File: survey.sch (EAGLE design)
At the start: 18 parts

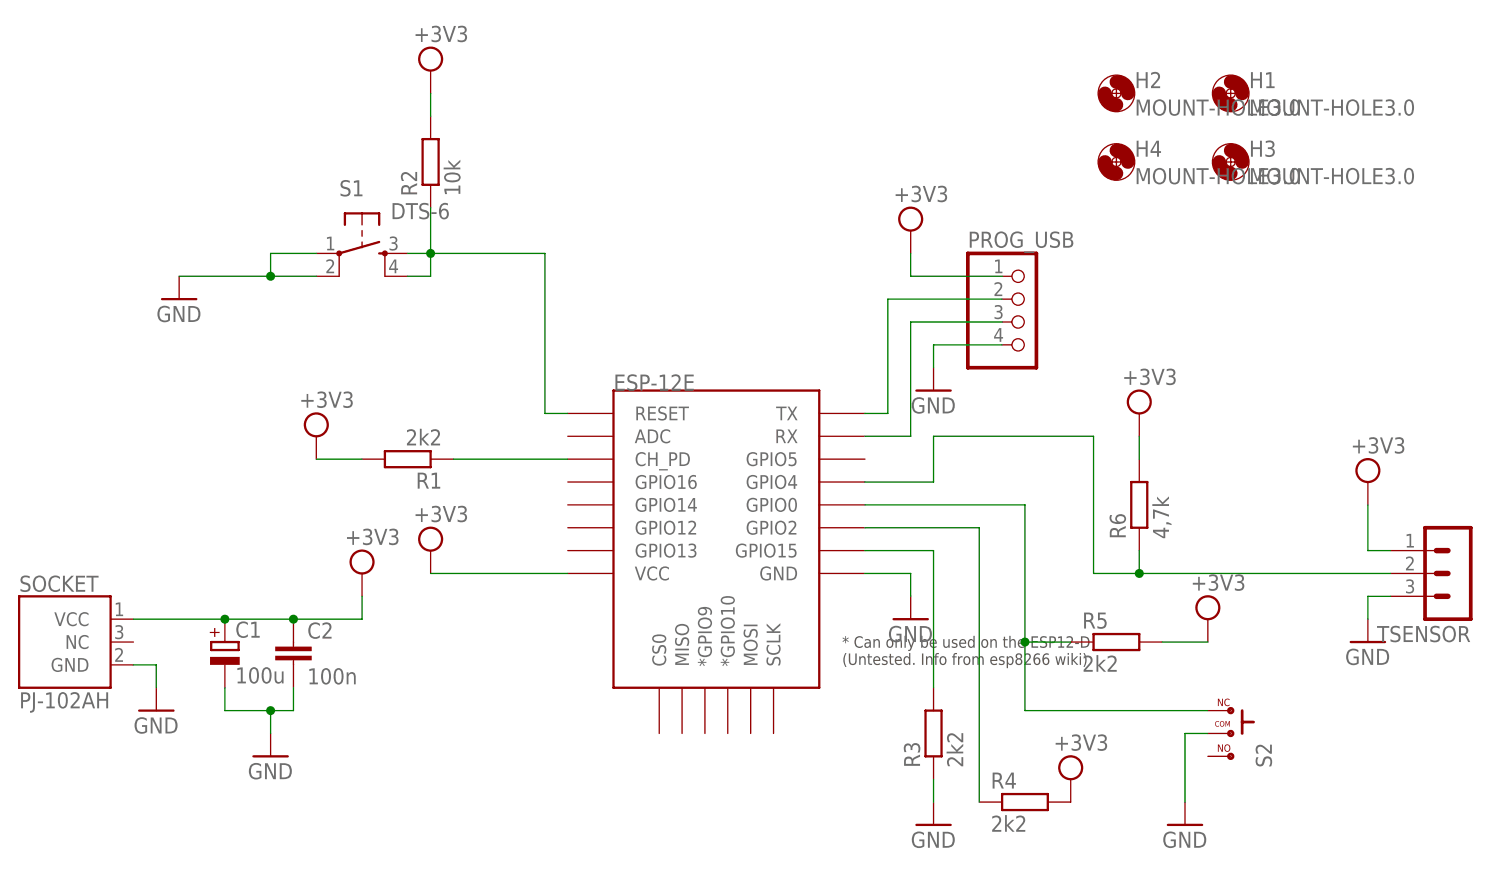
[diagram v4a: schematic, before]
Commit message: Changed some resistors from 10k for 2k2 and added resisors 100 to reset and gpio0 pin.
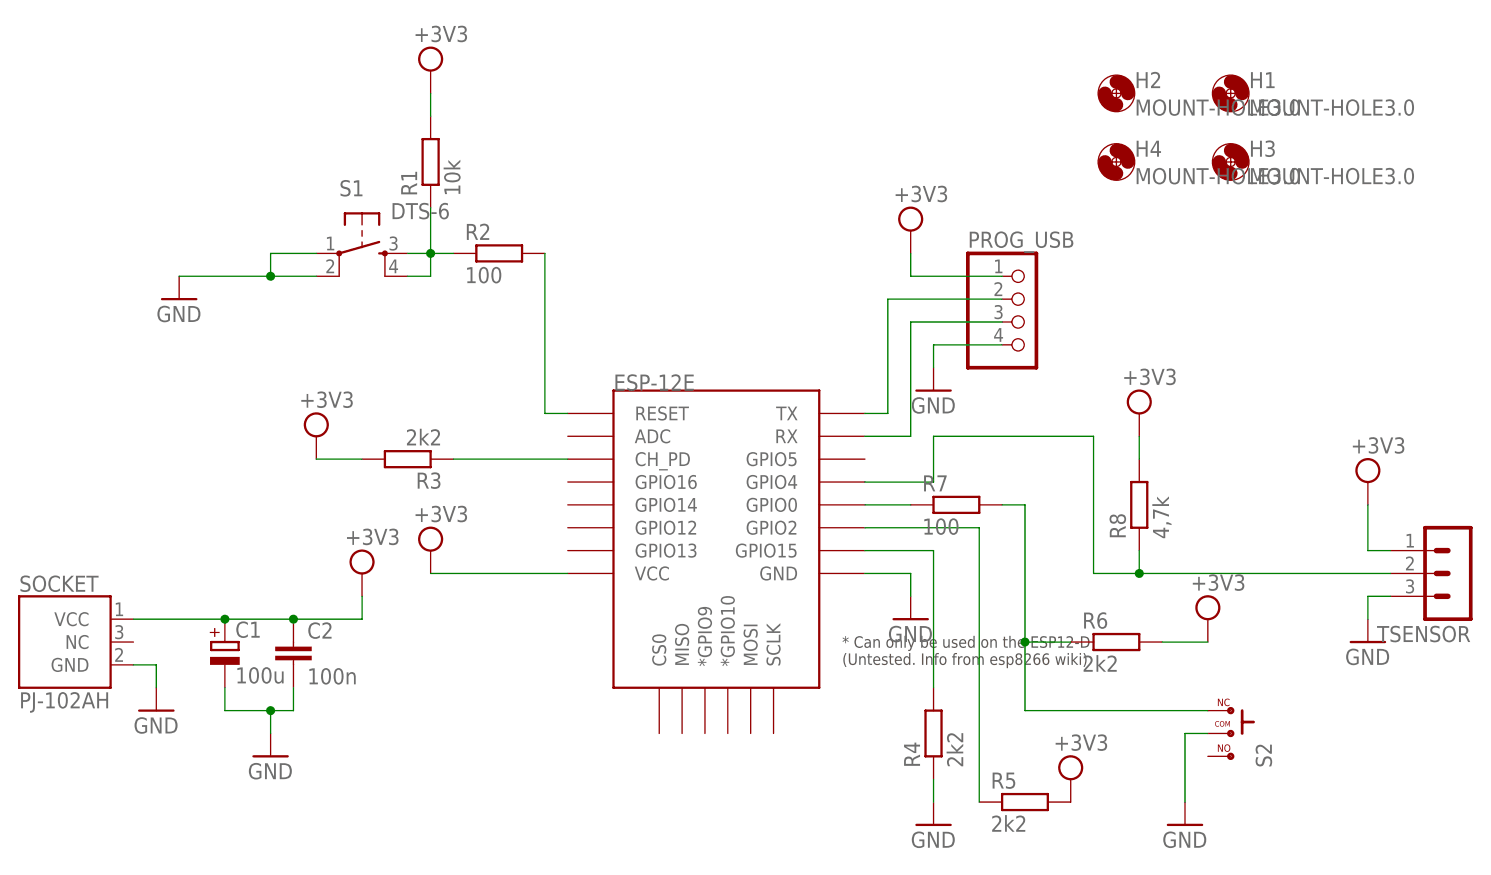
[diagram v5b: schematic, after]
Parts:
- added R7: 100, rcl:R-EU_0204/7
- added R8: 4,7k, rcl:R-EU_0204/7
- R1: value 2k2 -> 10k
- R2: value 10k -> 100
- R6: value 4,7k -> 2k2
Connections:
- new net N$10: ESP-12E.GPIO0, R7.1
- new net N$9: R1.1, R2.1, S1.3, S1.4
- net GND: now also R4.1; no longer R3.1
- net N$1: now also R5.1; no longer R4.1
- net N$2: now also R3.1; no longer R1.1
- net N$5: now also R8.1; no longer R6.1
- net N$6: now also R6.1, R7.2; no longer ESP-12E.GPIO0, R5.1
- net N$7: now also R4.2; no longer R3.2
- net N$8: now also R2.2; no longer R2.1, S1.3, S1.4
- net VCC: now also R3.2, R8.2; no longer R2.2, R4.2
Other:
- moved on the sheet: R1, R2, R3, R4, R5, R6
